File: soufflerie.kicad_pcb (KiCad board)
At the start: 4 copper layers, 100 x 120 mm, 66 parts, among them IC1 BMP390, IC2 SDP31, IC3 LM3940IMP-3.3, J1 MicroSD_Connector_503182-1852, J2 USB-C_12pin, J3 CON05, J4 CON05, J5 DB9_Male, J7 CON05, M2 PIXXILCD-25P4-CTP_FPC30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

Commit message: silkscreen
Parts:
- moved J5 0.50 mm to (175.6, 43.8)
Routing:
- net GND: track 128.4 -> 130.2 mm
- net /RS485B: track 26.2 -> 26.7 mm
- net /RS485A: track 13.1 -> 12.6 mm
- added copper zone on B.Cu, net GND
- added copper zone on F.Cu, net GND
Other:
- board text added: "3.3V"
- board text added: "5V"
- board text added: "BOOT0"
- board text added: "GND"
- board text added: "I2C2"
- board text added: "LCD_RX"
- board text added: "LCD_TX"
- board text added: "NRST"
- board text added: "RS485"
- board text added: "RX"
- board text added: "RX_485"
- board text added: "SCL"
- board text added: "SCL1"
- board text added: "SDA"
- board text added: "SDA1"
- board text added: "SWD"
- board text added: "SWDCLK"
- board text added: "SWDIO"
- board text added: "TX"
- board text added: "TX_485"
- board text added: "UART6"

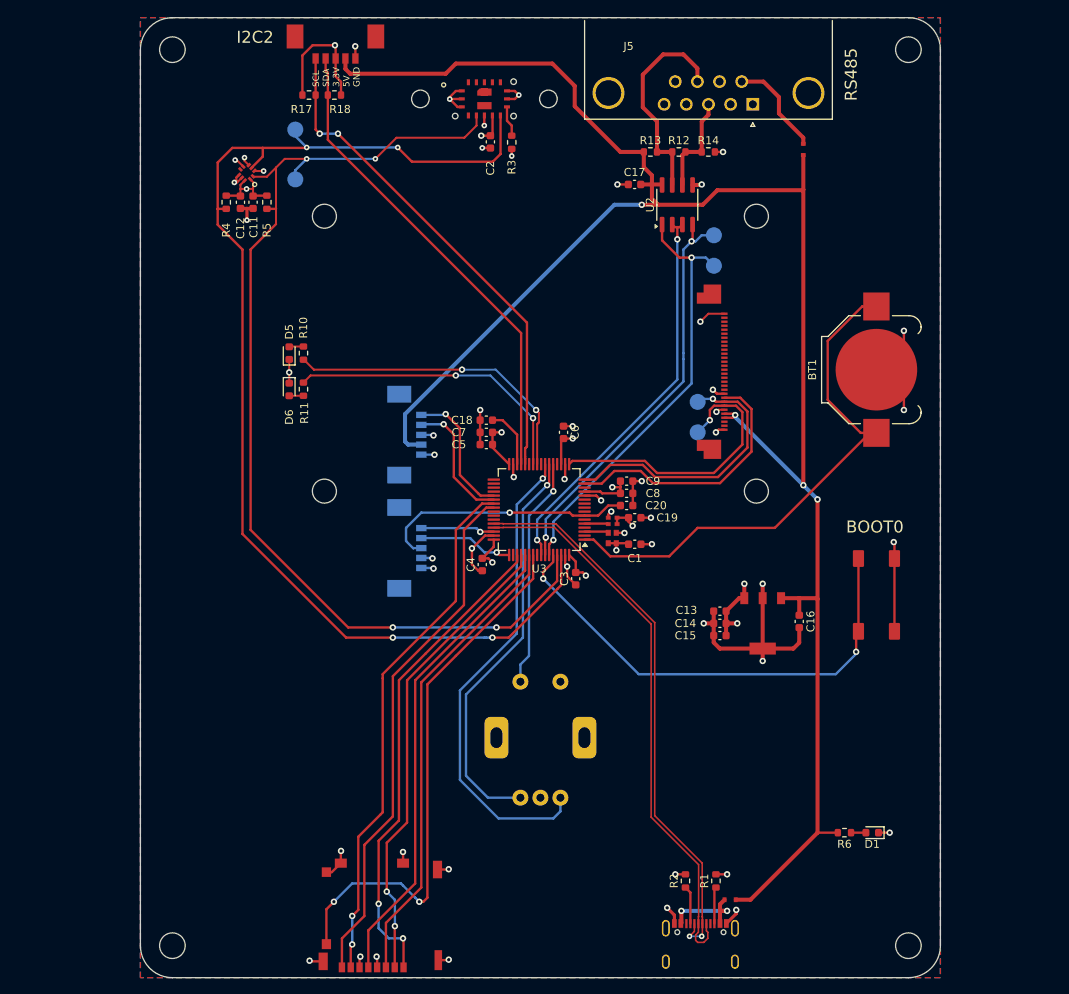
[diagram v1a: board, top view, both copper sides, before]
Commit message: connect SDP31 DIE pad
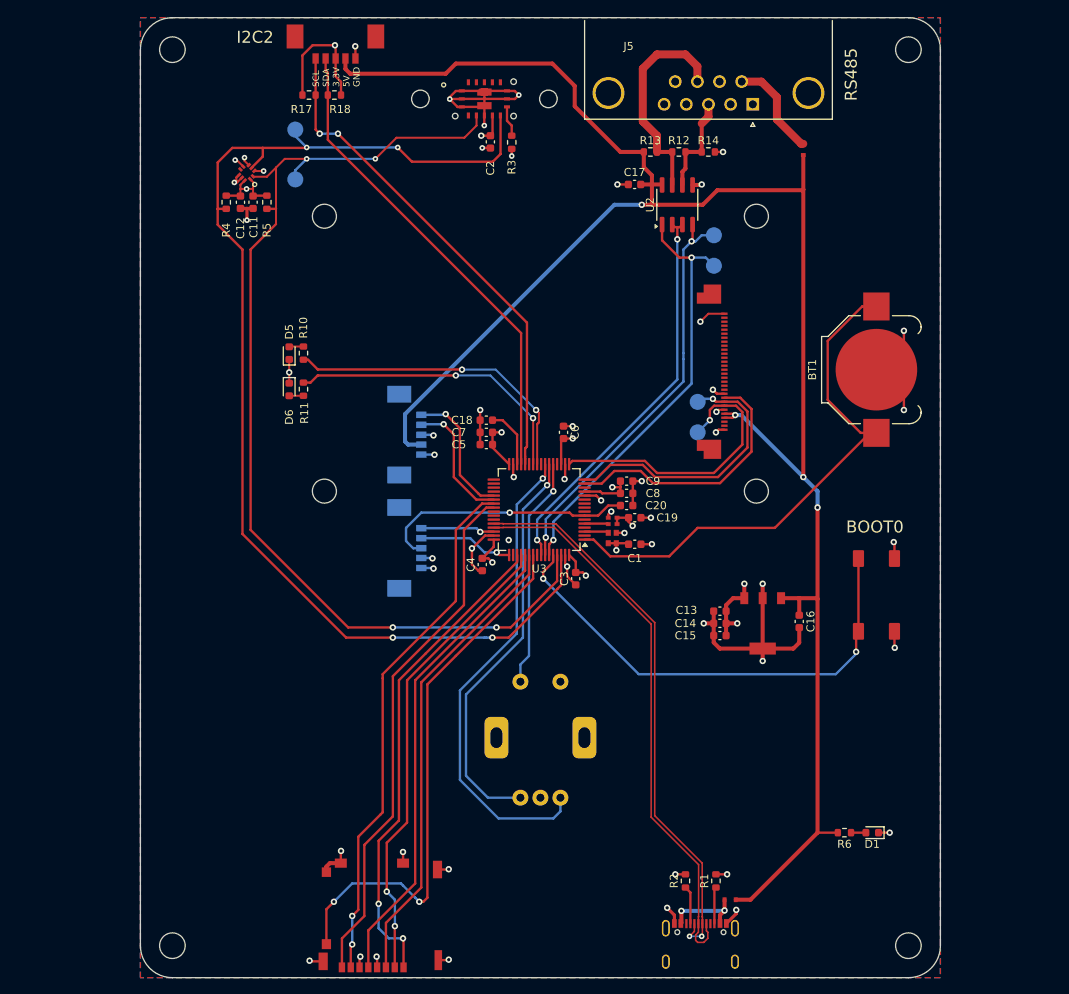
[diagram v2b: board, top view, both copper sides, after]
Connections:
- IC2 pad DP: unconnected-(IC2-DiePad-PadDP)_0 -> GND
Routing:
- net GND: track 130.2 -> 147.9 mm, vias 48 -> 49
- net +3V3: track 88.3 -> 81.7 mm, vias 17 -> 18
- net /USB_VBUS: track 11.4 -> 10.2 mm
- net +5V: track 246.1 -> 245.3 mm
- net /RS485B: track 26.7 -> 27.3 mm

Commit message: add sensor probe
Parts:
- added C10: 100n, Capacitor_SMD:C_0603_1608Metric, F.Cu at (91.8, 129.7)
- added J6: CON04, _Connectors_GRZ:PicoBlade_53398-0471, F.Cu at (89.8, 85.4)
- added R15: 4.7k, Resistor_SMD:R_0603_1608Metric, F.Cu at (88.5, 92.1)
- added R16: 4.7k, Resistor_SMD:R_0603_1608Metric, F.Cu at (88.5, 95.2)
- added U1: SHT4x, Sensor_Humidity:Sensirion_DFN-4_1.5x1.5mm_P0.8mm_SHT4x_NoCentralPad, F.Cu at (89.8, 132.9)
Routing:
- net +3V3_EXT: track 0.00 -> 55.6 mm, vias 0 -> 2
- net /SDA_EXT: track 0.00 -> 48.5 mm, vias 0 -> 2
- net /SCL_EXT: track 0.00 -> 46.9 mm
- net GND_2: track 0.00 -> 4.13 mm, vias 0 -> 3
- added copper zone on B.Cu, net GND_2
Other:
- board size 100 x 120 mm -> 115.5 x 120 mm

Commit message: add a few vias
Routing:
- net +3V3: track 81.7 -> 79.5 mm
- net GND: vias 49 -> 53
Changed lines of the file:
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@@
 		(tags "resistor")
 		(property "Reference" "R16"
-			(at 0 -1.43 90)
+			(at 3.063 0.019 180)
 			(layer "F.SilkS")
 			(effects
@@
 		(tags "capacitor")
 		(property "Reference" "C10"
-			(at 0 -1.43 270)
+			(at 2.917 -0.571 0)
 			(layer "F.SilkS")
 			(effects
@@
 		(tags "resistor")
 		(property "Reference" "R15"
-			(at 0 -1.43 270)
+			(at 2.388 0.231 0)
 			(layer "F.SilkS")
 			(effects
@@
 		(tags "DFN NoLead")
 		(property "Reference" "U1"
-			(at 0 -1.7 90)
+			(at -2.407 0.058 180)
 			(layer "F.SilkS")
 			(effects
@@
 	)
 	(via
+		(at 127.75 48)
+		(size 1)
+		(drill 0.6)
+		(layers "F.Cu" "B.Cu")
+		(free yes)
+		(net 1)
+	)
+	(via
 		(at 126.492 150.368)
 		(size 0.8)
@@
 	)
 	(via
+		(at 158.5 101.75)
+		(size 1)
+		(drill 0.6)
+		(layers "F.Cu" "B.Cu")
+		(free yes)
+		(net 1)
+	)
+	(via
 		(at 131.826 137.287)
 		(size 0.8)
@@
 	)
 	(via
+		(at 180.5 53.25)
+		(size 1)
+		(drill 0.6)
+		(layers "F.Cu" "B.Cu")
+		(free yes)
+		(net 1)
+	)
+	(via
 		(at 141.986 46.482)
 		(size 0.7)
@@
 	)
 	(via
+		(at 125.75 41.5)
+		(size 1)
+		(drill 0.6)
+		(layers "F.Cu" "B.Cu")
+		(free yes)
+		(net 1)
+	)
+	(via
 		(at 159.512 97.409)
 		(size 0.8)
@@
 	)
 	(segment
-		(start 143.017 45.239)
-		(end 143.017 47.483)
-		(width 0.3)
-		(layer "F.Cu")
-		(net 3)
-	)
-	(segment
 		(start 151.594 85.909)
 		(end 151.594 88.813)
@@
 	)
 	(segment
-		(start 90.951 99.573)
-		(end 90.951 130.429)
-		(width 0.3)
-		(layer "F.Cu")
-		(net 81)
-	)
-	(segment
 		(start 89.408 134.285)
 		(end 89.681 134.558)
@@
 	)
 	(segment
-		(start 90.939 93.726)
-		(end 90.939 99.561)
+		(start 90.951 130.429)
+		(end 90.951 131.256)
 		(width 0.3)
 		(layer "F.Cu")
@@
 	)
 	(segment
-		(start 90.951 130.429)
-		(end 90.951 131.256)
+		(start 90.939 93.726)
+		(end 90.939 130.417)
 		(width 0.3)
 		(layer "F.Cu")
@@
 	)
 	(segment
-		(start 90.939 99.561)
-		(end 90.951 99.573)
-		(width 0.3)
-		(layer "F.Cu")
-		(net 81)
-	)
-	(segment
 		(start 89.681 134.558)
 		(end 90.697 134.558)
@@
 	)
 	(segment
-		(start 90.939 99.561)
-		(end 90.932 99.568)
+		(start 90.697 134.558)
+		(end 91.708 133.547)
 		(width 0.3)
 		(layer "F.Cu")
@@
 	)
 	(segment
-		(start 90.697 134.558)
-		(end 91.708 133.547)
+		(start 90.939 130.417)
+		(end 90.951 130.429)
 		(width 0.3)
 		(layer "F.Cu")

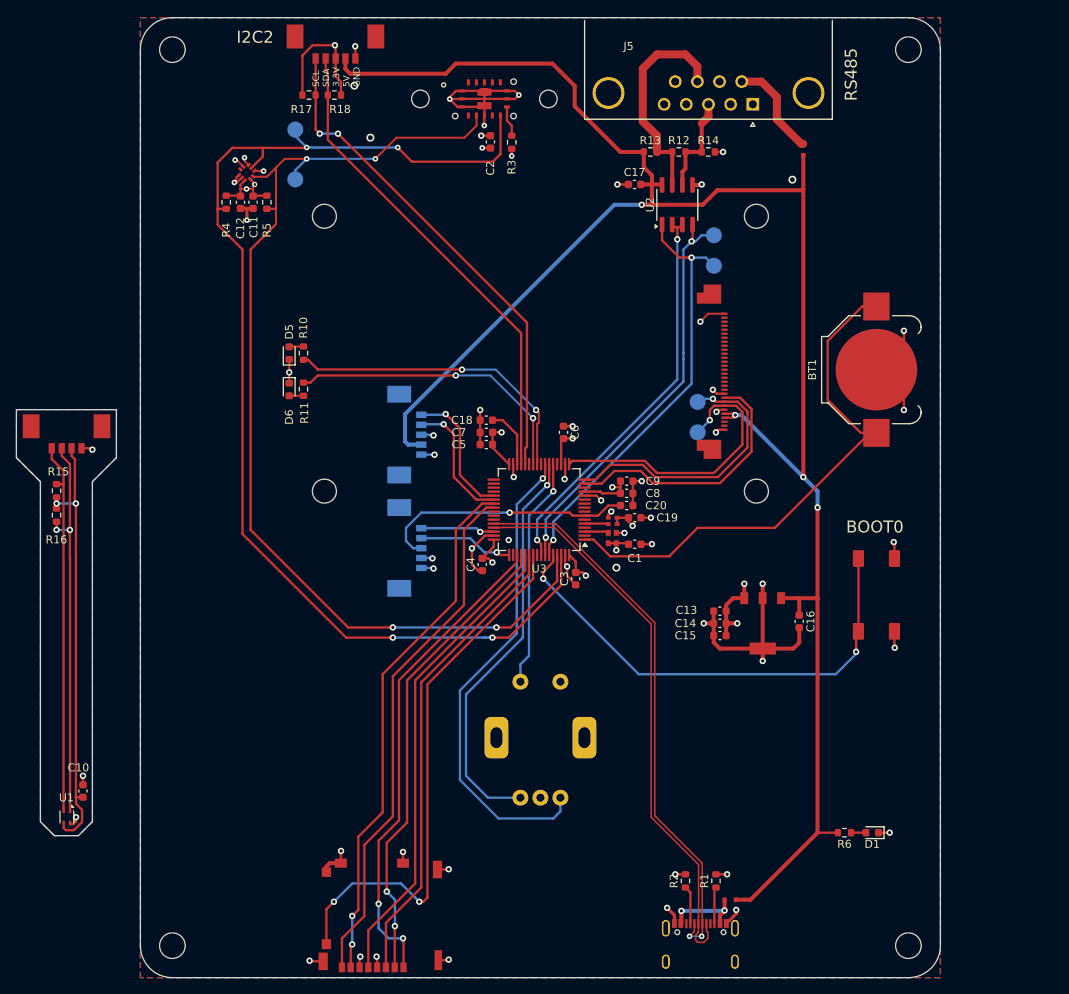
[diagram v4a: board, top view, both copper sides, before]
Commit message: fix unconnected pad.
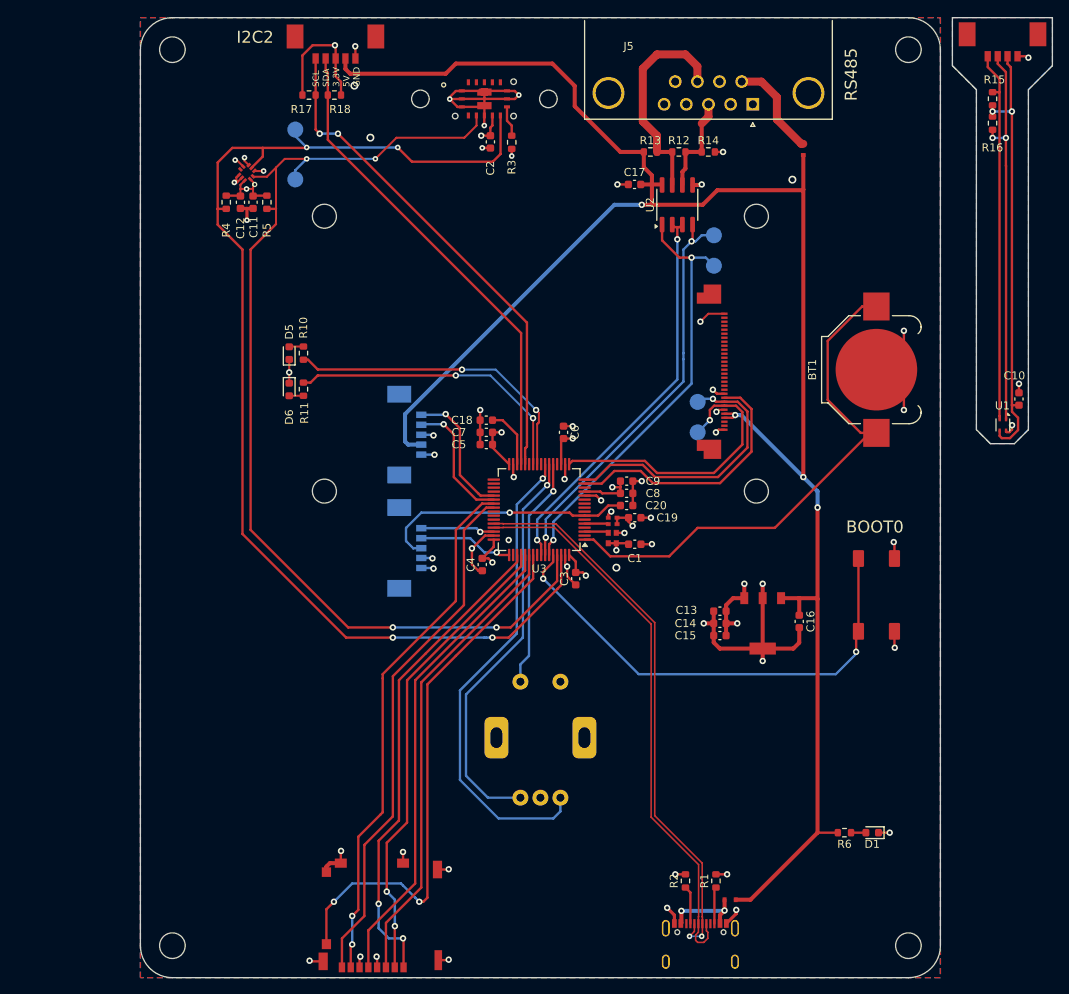
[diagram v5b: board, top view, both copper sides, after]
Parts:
- moved C10 126.8 mm to (208.8, 80.7)
- moved J6 126.8 mm to (206.8, 36.4)
- moved R15 126.8 mm to (205.5, 43.1)
- moved R16 126.8 mm to (205.5, 46.2)
- moved U1 126.8 mm to (206.8, 83.9)
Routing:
- net +3V3: track 79.5 -> 82.1 mm
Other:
- board size 115.5 x 120 mm -> 114 x 120 mm
